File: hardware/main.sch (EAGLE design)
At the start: 7 parts, among them X1 JACK, X2 POWER

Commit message: Added A4 frame to schema
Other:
- moved on the sheet: ARDUINO, R1, R2, S2, WIFLY, X1-1, X1-2, X1-3, X2-1, X2-2

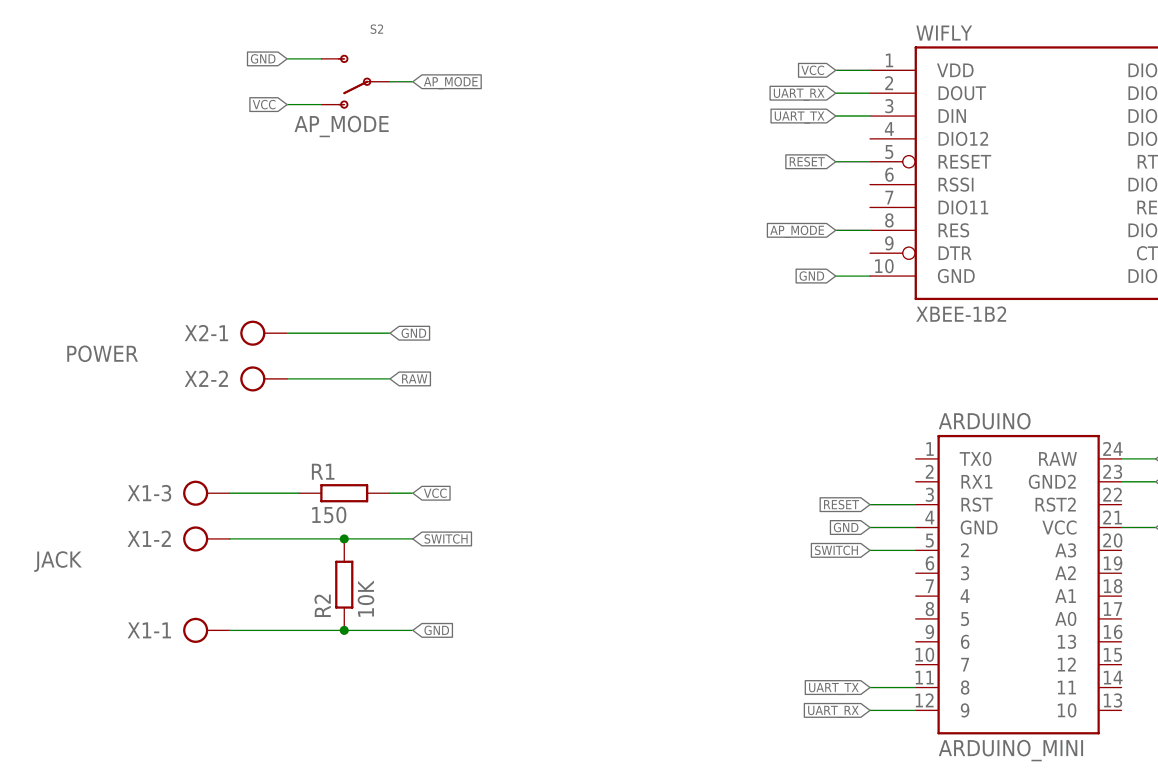
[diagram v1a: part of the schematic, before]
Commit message: Añadidos cambios sobre el hardware y el firmware del prototipo final.
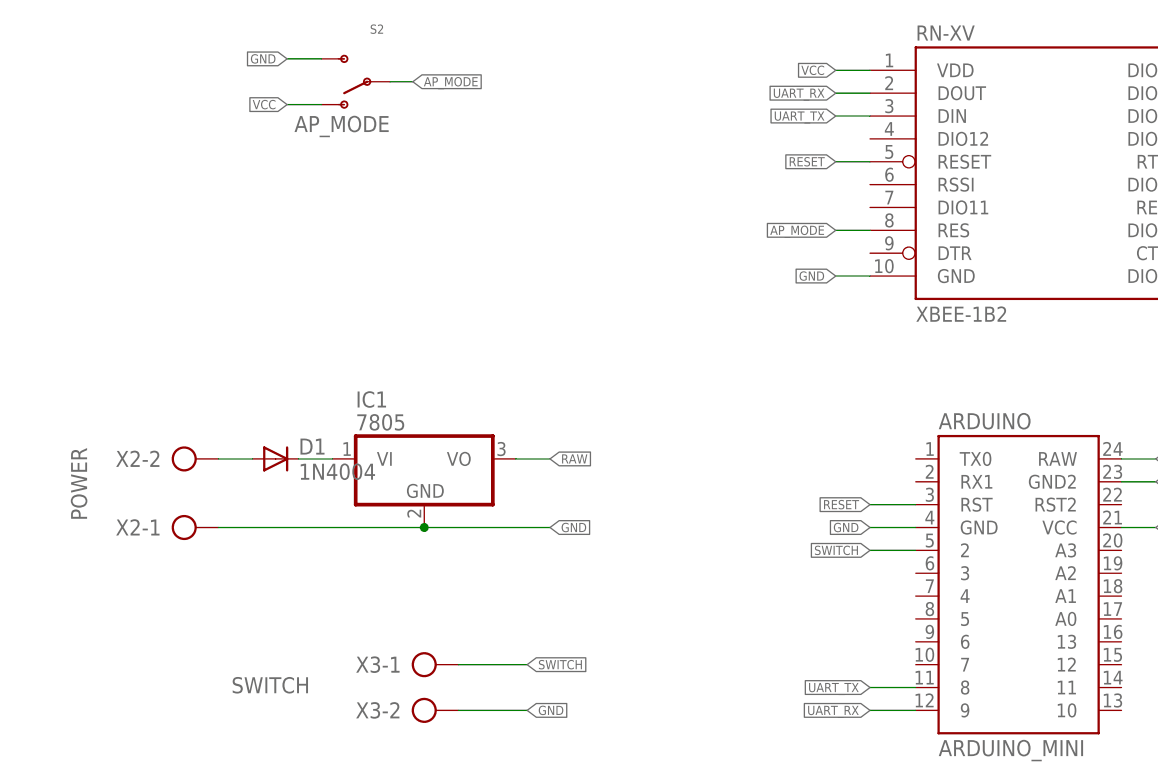
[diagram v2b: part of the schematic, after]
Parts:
- removed R1: 150, resistor:R-EU_0204/7
- removed R2: 10K, resistor:R-EU_0204/7
- removed X1: JACK, con-ptr500:AK500/3
- added D1: 1N4004, diode:1N4004
- added IC1: 7805, linear:786TV
- added X3: SWITCH, con-ptr500:AK500/2
- renumbered WIFLY to RN-XV
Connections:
- new net N$2: D1.C, IC1.VI
- net GND: now also IC1.GND, X3-2.KL; no longer R2.1, X1-1.KL
- net N$1: now also D1.A, X2-2.KL; no longer R1.1, X1-3.KL
- net RAW: now also IC1.VO; no longer X2-2.KL
- net SWITCH: now also X3-1.KL; no longer R2.2, X1-2.KL
- net VCC: no longer R1.2
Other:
- moved on the sheet: X2-1, X2-2
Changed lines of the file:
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@@
 </classes>
 <parts>
-<part name="X1" library="con-ptr500" deviceset="AK500/3" device="" value="JACK"/>
 <part name="ARDUINO" library="SparkFun-Boards" deviceset="ARDUINO_MINI" device=""/>
 <part name="X2" library="con-ptr500" deviceset="AK500/2" device="" value="POWER"/>
-<part name="WIFLY" library="SparkFun-RF" deviceset="XBEE-1" device="B2"/>
+<part name="RN-XV" library="SparkFun-RF" deviceset="XBEE-1" device="B2"/>
 <part name="S2" library="SparkFun-Electromechanical" deviceset="SWITCH-SPDT" device="PTH" value="AP_MODE"/>
-<part name="R1" library="resistor" deviceset="R-EU_" device="0204/7" value="150"/>
-<part name="R2" library="resistor" deviceset="R-EU_" device="0204/7" value="10K"/>
 <part name="FRAME1" library="frames" deviceset="A4L-LOC" device=""/>
+<part name="IC1" library="linear" deviceset="78*" device="TV" technology="6" value="7805"/>
+<part name="X3" library="con-ptr500" deviceset="AK500/2" device="" value="SWITCH">
+<attribute name="MF" value=""/>
+<attribute name="MPN" value=""/>
+<attribute name="OC_FARNELL" value="unknown"/>
+<attribute name="OC_NEWARK" value="unknown"/>
+</part>
+<part name="D1" library="diode" deviceset="1N4004" device=""/>
 </parts>
 <sheets>
@@
 </plain>
 <instances>
-<instance part="X1" gate="-1" x="71.12" y="64.77"/>
-<instance part="X1" gate="-2" x="71.12" y="74.93"/>
-<instance part="X1" gate="-3" x="71.12" y="80.01" smashed="yes">
-<attribute name="NAME" x="69.85" y="80.899" size="1.778" layer="95" rot="R180"/>
-<attribute name="VALUE" x="59.69" y="73.533" size="1.778" layer="96" rot="R180"/>
+<instance part="ARDUINO" gate="G$1" x="162.56" y="71.12"/>
+<instance part="X2" gate="-1" x="69.85" y="76.2"/>
+<instance part="X2" gate="-2" x="69.85" y="83.82" smashed="yes">
+<attribute name="NAME" x="68.58" y="84.709" size="1.778" layer="95" rot="R180"/>
+<attribute name="VALUE" x="58.547" y="85.09" size="1.778" layer="96" rot="R270"/>
 </instance>
-<instance part="ARDUINO" gate="G$1" x="162.56" y="71.12"/>
-<instance part="X2" gate="-1" x="77.47" y="97.79"/>
-<instance part="X2" gate="-2" x="77.47" y="92.71" smashed="yes">
-<attribute name="NAME" x="76.2" y="93.599" size="1.778" layer="95" rot="R180"/>
-<attribute name="VALUE" x="66.04" y="96.393" size="1.778" layer="96" rot="R180"/>
-</instance>
-<instance part="WIFLY" gate="G$1" x="167.64" y="116.84"/>
+<instance part="RN-XV" gate="G$1" x="167.64" y="116.84"/>
 <instance part="S2" gate="1" x="91.44" y="125.73" smashed="yes" rot="R180">
 <attribute name="NAME" x="93.345" y="132.08" size="1.016" layer="95" font="vector" ratio="10" rot="R180"/>
 <attribute name="VALUE" x="93.98" y="121.92" size="1.778" layer="96" rot="R180"/>
 </instance>
-<instance part="R1" gate="G$1" x="88.9" y="80.01"/>
-<instance part="R2" gate="G$1" x="88.9" y="69.85" rot="R90"/>
 <instance part="FRAME1" gate="G$1" x="0" y="0"/>
+<instance part="IC1" gate="A1" x="97.79" y="83.82"/>
+<instance part="X3" gate="-1" x="96.52" y="60.96"/>
+<instance part="X3" gate="-2" x="96.52" y="55.88" smashed="yes">
+<attribute name="NAME" x="95.25" y="56.769" size="1.778" layer="95" rot="R180"/>
+<attribute name="VALUE" x="85.09" y="59.563" size="1.778" layer="96" rot="R180"/>
+</instance>
+<instance part="D1" gate="1" x="81.28" y="83.82"/>
 </instances>
 <busses>
@@
 <label x="143.51" y="124.46" size="1.016" layer="95" rot="R180" xref="yes"/>
 <wire x1="147.32" y1="124.46" x2="143.51" y2="124.46" width="0.1524" layer="91"/>
-<pinref part="WIFLY" gate="G$1" pin="DOUT"/>
+<pinref part="RN-XV" gate="G$1" pin="DOUT"/>
 </segment>
 <segment>
@@
 <wire x1="143.51" y1="121.92" x2="147.32" y2="121.92" width="0.1524" layer="91"/>
 <label x="143.51" y="121.92" size="1.016" layer="95" rot="R180" xref="yes"/>
-<pinref part="WIFLY" gate="G$1" pin="DIN"/>
+<pinref part="RN-XV" gate="G$1" pin="DIN"/>
 </segment>
 <segment>
@@
 <segment>
 <pinref part="X2" gate="-1" pin="KL"/>
-<wire x1="82.55" y1="97.79" x2="93.98" y2="97.79" width="0.1524" layer="91"/>
-<label x="93.98" y="97.79" size="1.016" layer="95" xref="yes"/>
+<wire x1="74.93" y1="76.2" x2="97.79" y2="76.2" width="0.1524" layer="91"/>
+<label x="111.76" y="76.2" size="1.016" layer="95" xref="yes"/>
+<pinref part="IC1" gate="A1" pin="GND"/>
+<wire x1="97.79" y1="76.2" x2="111.76" y2="76.2" width="0.1524" layer="91"/>
+<junction x="97.79" y="76.2"/>
 </segment>
 <segment>
 <wire x1="147.32" y1="104.14" x2="143.51" y2="104.14" width="0.1524" layer="91"/>
-<pinref part="WIFLY" gate="G$1" pin="GND"/>
+<pinref part="RN-XV" gate="G$1" pin="GND"/>
 <label x="143.51" y="104.14" size="1.016" layer="95" rot="R180" xref="yes"/>
 <wire x1="86.36" y1="128.27" x2="82.55" y2="128.27" width="0.1524" layer="91"/>
@@
 </segment>
 <segment>
-<pinref part="R2" gate="G$1" pin="1"/>
-<wire x1="88.9" y1="64.77" x2="96.52" y2="64.77" width="0.1524" layer="91"/>
-<label x="96.52" y="64.77" size="1.016" layer="95" xref="yes"/>
-<pinref part="X1" gate="-1" pin="KL"/>
-<wire x1="88.9" y1="64.77" x2="76.2" y2="64.77" width="0.1524" layer="91"/>
-<junction x="88.9" y="64.77"/>
+<wire x1="101.6" y1="55.88" x2="109.22" y2="55.88" width="0.1524" layer="91"/>
+<pinref part="X3" gate="-2" pin="KL"/>
+<label x="109.22" y="55.88" size="1.016" layer="95" xref="yes"/>
 </segment>
 </net>
@@
 <segment>
 <wire x1="143.51" y1="127" x2="147.32" y2="127" width="0.1524" layer="91"/>
-<pinref part="WIFLY" gate="G$1" pin="VDD"/>
+<pinref part="RN-XV" gate="G$1" pin="VDD"/>
 <label x="143.51" y="127" size="1.016" layer="95" rot="R180" xref="yes"/>
 <wire x1="82.55" y1="123.19" x2="86.36" y2="123.19" width="0.1524" layer="91"/>
 <pinref part="S2" gate="1" pin="O"/>
 <label x="82.55" y="123.19" size="1.016" layer="95" rot="R180" xref="yes"/>
-</segment>
-<segment>
-<pinref part="R1" gate="G$1" pin="2"/>
-<wire x1="93.98" y1="80.01" x2="96.52" y2="80.01" width="0.1524" layer="91"/>
-<label x="96.52" y="80.01" size="1.016" layer="95" xref="yes"/>
 </segment>
 </net>
@@
 </segment>
 <segment>
-<pinref part="X2" gate="-2" pin="KL"/>
-<wire x1="82.55" y1="92.71" x2="93.98" y2="92.71" width="0.1524" layer="91"/>
-<label x="93.98" y="92.71" size="1.016" layer="95" xref="yes"/>
+<pinref part="IC1" gate="A1" pin="VO"/>
+<wire x1="107.95" y1="83.82" x2="111.76" y2="83.82" width="0.1524" layer="91"/>
+<label x="111.76" y="83.82" size="1.016" layer="95" xref="yes"/>
 </segment>
 </net>
@@
 </segment>
 <segment>
-<pinref part="WIFLY" gate="G$1" pin="RESET"/>
+<pinref part="RN-XV" gate="G$1" pin="RESET"/>
 <wire x1="147.32" y1="116.84" x2="143.51" y2="116.84" width="0.1524" layer="91"/>
 <label x="143.51" y="116.84" size="1.016" layer="95" rot="R180" xref="yes"/>
@@
 <net name="AP_MODE" class="0">
 <segment>
-<pinref part="WIFLY" gate="G$1" pin="RES@8"/>
+<pinref part="RN-XV" gate="G$1" pin="RES@8"/>
 <wire x1="147.32" y1="109.22" x2="143.51" y2="109.22" width="0.1524" layer="91"/>
 <label x="143.51" y="109.22" size="1.016" layer="95" rot="R180" xref="yes"/>
@@
 </segment>
 <segment>
-<pinref part="X1" gate="-2" pin="KL"/>
-<wire x1="76.2" y1="74.93" x2="88.9" y2="74.93" width="0.1524" layer="91"/>
-<label x="96.52" y="74.93" size="1.016" layer="95" xref="yes"/>
-<pinref part="R2" gate="G$1" pin="2"/>
-<wire x1="88.9" y1="74.93" x2="96.52" y2="74.93" width="0.1524" layer="91"/>
-<junction x="88.9" y="74.93"/>
+<wire x1="101.6" y1="60.96" x2="109.22" y2="60.96" width="0.1524" layer="91"/>
+<pinref part="X3" gate="-1" pin="KL"/>
+<label x="109.22" y="60.96" size="1.016" layer="95" xref="yes"/>
+</segment>
+</net>
+<net name="N$2" class="0">
+<segment>
+<pinref part="IC1" gate="A1" pin="VI"/>
+<pinref part="D1" gate="1" pin="C"/>
+<wire x1="83.82" y1="83.82" x2="87.63" y2="83.82" width="0.1524" layer="91"/>
 </segment>
 </net>
 <net name="N$1" class="0">
 <segment>
-<pinref part="R1" gate="G$1" pin="1"/>
-<pinref part="X1" gate="-3" pin="KL"/>
-<wire x1="76.2" y1="80.01" x2="83.82" y2="80.01" width="0.1524" layer="91"/>
+<pinref part="D1" gate="1" pin="A"/>
+<pinref part="X2" gate="-2" pin="KL"/>
+<wire x1="74.93" y1="83.82" x2="78.74" y2="83.82" width="0.1524" layer="91"/>
 </segment>
 </net>
